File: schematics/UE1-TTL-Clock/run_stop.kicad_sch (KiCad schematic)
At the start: 16 parts, among them SW1 RUN, SW2 HALT, SW3 RESET, U1 74LS74, U5 74LS132, U6 74LS02

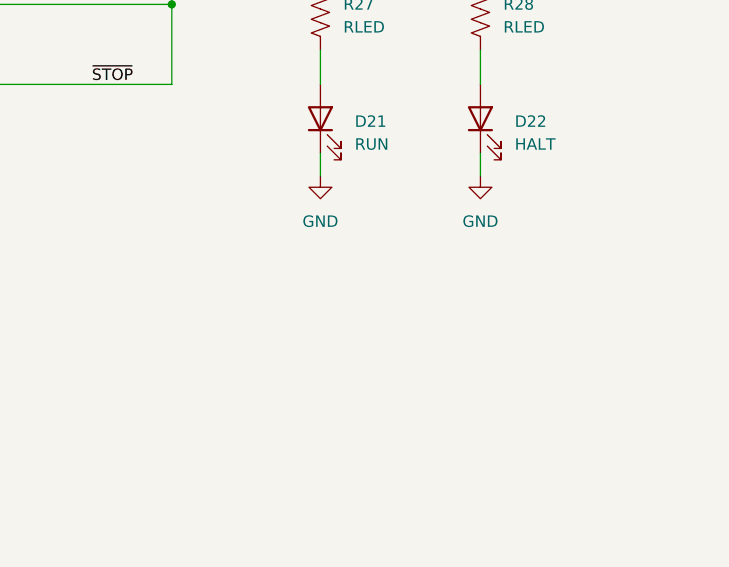
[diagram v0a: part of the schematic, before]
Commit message: Lay out clock board
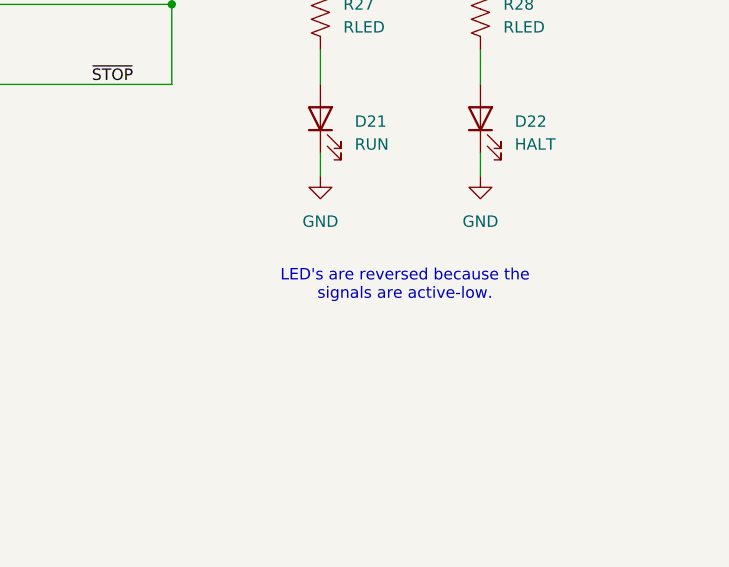
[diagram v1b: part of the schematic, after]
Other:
- note added: "LED's are reversed because the signals are active-low."
- title: UE1- TTL Clock and Diagnostics -> UE1-TTL Clock and Front Panel
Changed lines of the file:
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@@
 	(paper "A4")
 	(title_block
-		(title "UE1- TTL Clock and Diagnostics")
+		(title "UE1-TTL Clock and Front Panel")
 		(date "2025")
 		(rev "1")
@@
 		(effects
 			(font
+				(size 1.27 1.27)
+			)
+		)
+	)
+	(text "LED's are reversed because the\nsignals are active-low."
+		(exclude_from_sim no)
+		(at 215.138 116.332 0)
+		(effects
+			(font
